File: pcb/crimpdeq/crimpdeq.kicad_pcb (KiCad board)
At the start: 4 copper layers, 30 x 30 mm, 55 parts, among them J10 A-_Cable_Pad, J11 E+_Cable_Pad, J12 E-_Cable_Pad, J2 USB4105-GF-A, J5 B-_Cable_Pad, J6 SW+_Cable_Pad, J7 B+_Cable_Pad, J8 SW-_Cable_Pad, J9 A+_Cable_Pad, Q2 DMG3415U, U1 ESP32-C3-MINI-1, U2 MCP73831T-2ACI/OT, U3 ADS1220, U5 MAX17048G+T10, U6 SY8088

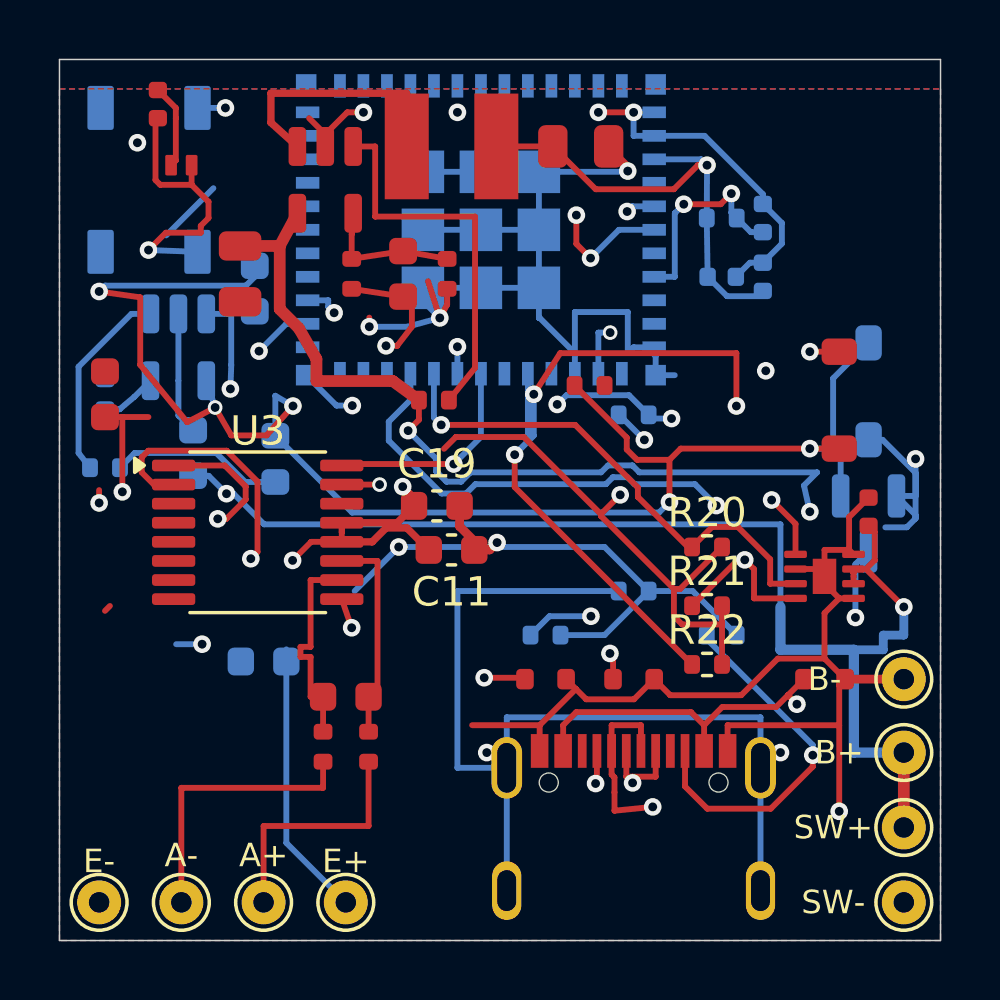
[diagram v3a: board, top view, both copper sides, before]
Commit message: fix: align prototype metadata and clean board annotations
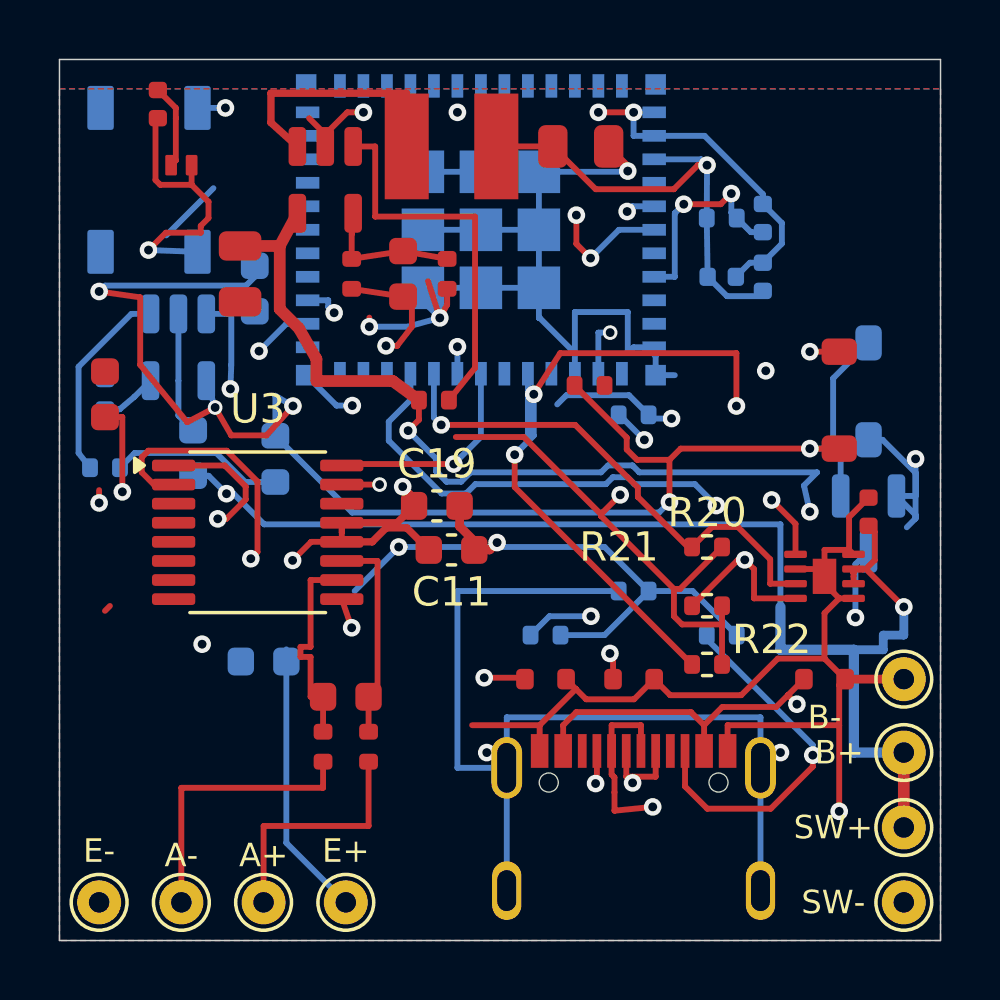
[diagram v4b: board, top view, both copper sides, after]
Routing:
- net +3V3: track 124.8 -> 122.5 mm
- net VSYS: track 41.1 -> 40.3 mm
- net Net-(D4-DIN): vias 4 -> 2
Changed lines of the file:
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@@
 		(sheetname "/")
 		(sheetfile "crimpdeq.kicad_sch")
+		(attr dnp)
 		(duplicate_pad_numbers_are_jumpers no)
 		(fp_circle
@@
 					(thickness 0.08)
 				)
-				(justify mirror)
 			)
 		)
@@
 					(thickness 0.06)
 				)
-				(justify mirror)
 			)
 		)
@@
 					(thickness 0.06)
 				)
-				(justify mirror)
 			)
 		)
@@
 		(tags "TSSOP SO JEDEC-MO-153-AB Texas_PW0016A Microchip-ST Toshiba-TSSOP16-P-0044-0.65A NXP-SOT403-1 Infineon-P-TSSOP-16-800")
 		(property "Reference" "U3"
-			(at 0 -3.45 0)
+			(at 0 -4.2 0)
 			(layer "F.SilkS")
 			(effects
@@
 		(tags "resistor")
 		(property "Reference" "R21"
-			(at 0 -1.17 0)
+			(at -3.0 -2.0 0)
 			(layer "F.SilkS")
 			(effects
@@
 					(thickness 0.04)
 				)
-				(justify mirror)
 			)
 		)
@@
 		(sheetname "/")
 		(sheetfile "crimpdeq.kicad_sch")
+		(attr dnp)
 		(duplicate_pad_numbers_are_jumpers no)
 		(fp_circle
@@
 					(thickness 0.04)
 				)
-				(justify mirror)
 			)
 		)
@@
 		(sheetname "/")
 		(sheetfile "crimpdeq.kicad_sch")
+		(attr dnp)
 		(duplicate_pad_numbers_are_jumpers no)
 		(fp_circle
@@
 					(thickness 0.15)
 				)
-				(justify mirror)
 			)
 		)
@@
 					(thickness 0.04)
 				)
-				(justify mirror)
 			)
 		)
@@
 			)
 		)
+		(attr dnp)
 		(duplicate_pad_numbers_are_jumpers no)
 		(fp_circle
@@
 		(sheetname "/")
 		(sheetfile "crimpdeq.kicad_sch")
+		(attr dnp)
 		(duplicate_pad_numbers_are_jumpers no)
 		(fp_circle
@@
 					(thickness 0.04)
 				)
-				(justify mirror)
 			)
 		)
@@
 					(thickness 0.04)
 				)
-				(justify mirror)
 			)
 		)
@@
 					(thickness 0.04)
 				)
-				(justify mirror)
 			)
 		)
@@
 					(thickness 0.06)
 				)
-				(justify mirror)
 			)
 		)
@@
 			)
 		)
+		(attr dnp)
 		(duplicate_pad_numbers_are_jumpers no)
 		(fp_circle
@@
 					(thickness 0.08)
 				)
-				(justify mirror)
 			)
 		)
@@
 		(tags "resistor")
 		(property "Reference" "R22"
-			(at 0 -1.17 0)
+			(at 2.2 -0.85 0)
 			(layer "F.SilkS")
 			(effects
@@
 		(sheetname "/")
 		(sheetfile "crimpdeq.kicad_sch")
+		(attr dnp)
 		(duplicate_pad_numbers_are_jumpers no)
 		(fp_circle
@@
 		(sheetname "/")
 		(sheetfile "crimpdeq.kicad_sch")
+		(attr dnp)
 		(duplicate_pad_numbers_are_jumpers no)
 		(fp_circle
@@
 					(thickness 0.06)
 				)
+				(justify mirror)
 			)
 		)
@@
 					(thickness 0.04)
 				)
+				(justify mirror)
 			)
 		)
@@
 					(thickness 0.06)
 				)
+				(justify mirror)
 			)
 		)
@@
 					(thickness 0.04)
 				)
+				(justify mirror)
 			)
 		)
@@
 					(thickness 0.04)
 				)
+				(justify mirror)
 			)
 		)
@@
 					(thickness 0.04)
 				)
+				(justify mirror)
 			)
 		)
@@
 					(thickness 0.04)
 				)
+				(justify mirror)
 			)
 		)
@@
 					(thickness 0.04)
 				)
+				(justify mirror)
 			)
 		)
@@
 					(thickness 0.04)
 				)
+				(justify mirror)
 			)
 		)
@@
 					(thickness 0.06)
 				)
+				(justify mirror)
 			)
 		)
@@
 					(thickness 0.06)
 				)
+				(justify mirror)
 			)
 		)
@@
 					(thickness 0.04)
 				)
+				(justify mirror)
 			)
 		)
@@
 	)
 	(gr_text "B-"
-		(at 153.5 73.5 0)
+		(at 153.5 74.8 0)
 		(layer "F.SilkS")
 		(effects
@@
 	)
 	(gr_text "E-"
-		(at 128.8 79.7 0)
+		(at 128.8 79.35 0)
 		(layer "F.SilkS")
 		(effects
@@
 	)
 	(gr_text "E+"
-		(at 137.2 79.7 0)
+		(at 137.2 79.35 0)
 		(layer "F.SilkS")
 		(effects
@@
 	)
 	(segment
-		(start 140.946 65.2556)
-		(end 140.544 65.6573)
-		(width 0.2)
-		(layer "F.Cu")
-		(net "+3V3")
-	)
-	(segment
 		(start 132.525 57.2436)
 		(end 131.95 56.6686)
@@
 	)
 	(segment
-		(start 129.591 64.575)
-		(end 130.48 64.575)
-		(width 0.2)
-		(layer "F.Cu")
-		(net "+3V3")
-	)
-	(segment
 		(start 131.073 58.2984)
 		(end 132.26 58.2984)
@@
 	)
 	(segment
-		(start 131.422 72.31)
-		(end 132.307 72.31)
-		(width 0.2)
-		(layer "B.Cu")
-		(net "+3V3")
-	)
-	(segment
 		(start 149.3 55.8)
 		(end 149.5 56)
@@
 	)
 	(segment
-		(start 156.302 68.3298)
-		(end 155.57 68.3298)
-		(width 0.2)
-		(layer "B.Cu")
-		(net "VSYS")
-	)
-	(segment
 		(start 153.247 66.4591)
 		(end 152.8 66.906099)
@@
 		(size 0.6)
 		(drill 0.3)
-		(layers "F.Cu" "B.Cu")
-		(net "Net-(D4-DIN)")
-	)
-	(via
-		(at 144.398 64.1454)
-		(size 0.6)
-		(drill 0.3)
-		(layers "F.Cu" "B.Cu")
-		(net "Net-(D4-DIN)")
-	)
-	(via
-		(at 130.103 55.2355)
-		(size 0.6)
-		(drill 0.3)

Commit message: fix: remove queued dangling PCB objects
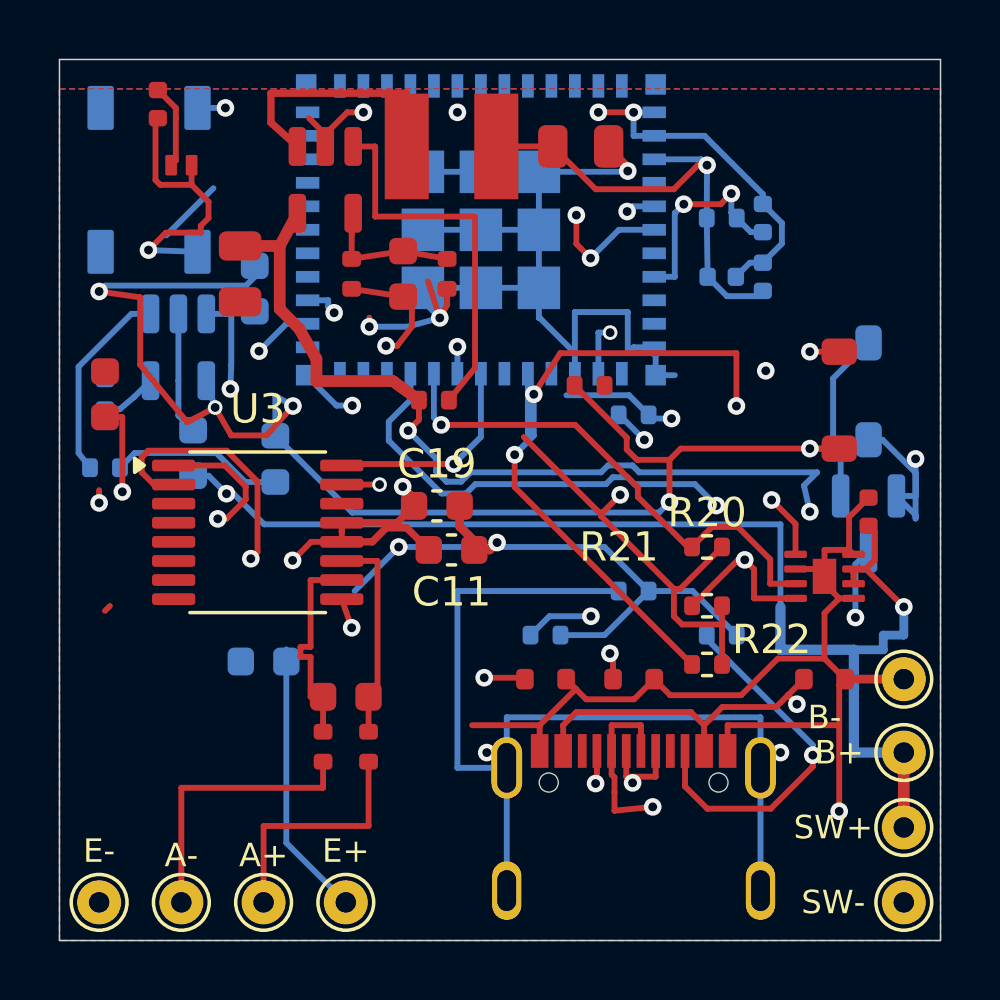
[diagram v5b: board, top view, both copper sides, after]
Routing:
- net +3V3: track 122.5 -> 120.2 mm, vias 9 -> 8
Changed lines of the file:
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@@
-	)
-	(segment
-		(start 143.26 65.2556)
-		(end 140.946 65.2556)
-		(width 0.2)
-		(layer "F.Cu")
-		(net "+3V3")
 	)
 	(segment
@@
 		(net "+3V3")
 	)
-	(via
-		(at 132.307 72.31)
-		(size 0.6)
-		(drill 0.3)
-		(layers "F.Cu" "B.Cu")
-		(net "+3V3")
-	)
 	(segment
 		(start 132.15 58.95)
@@
 	)
 	(segment
-		(start 156.6 68.031)
-		(end 156.302 68.3298)
-		(width 0.2)
-		(layer "B.Cu")
-		(net "VSYS")
-	)
-	(segment
 		(start 140.628 66.7771)
 		(end 140.275 66.4245)
@@
 		(width 0.2)
 		(layer "B.Cu")
-		(net "Net-(D4-DIN)")
-	)
-	(segment
-		(start 144.398 64.1454)
-		(end 144.711 63.8327)
-		(width 0.2)
-		(layer "B.Cu")

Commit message: feat: Prepare missing items
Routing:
- net +3V3: track 120.2 -> 116.5 mm
- net Net-(D4-DIN): track 34.2 -> 32.0 mm
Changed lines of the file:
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@@
 		(sheetname "/")
 		(sheetfile "crimpdeq.kicad_sch")
-		(attr dnp)
+		(attr exclude_from_pos_files dnp)
 		(duplicate_pad_numbers_are_jumpers no)
 		(fp_circle
@@
 		(sheetname "/")
 		(sheetfile "crimpdeq.kicad_sch")
-		(attr dnp)
+		(attr exclude_from_pos_files dnp)
 		(duplicate_pad_numbers_are_jumpers no)
 		(fp_circle
@@
 		(sheetname "/")
 		(sheetfile "crimpdeq.kicad_sch")
-		(attr dnp)
+		(attr exclude_from_pos_files dnp)
 		(duplicate_pad_numbers_are_jumpers no)
 		(fp_circle
@@
 			)
 		)
-		(attr dnp)
+		(attr exclude_from_pos_files dnp)
 		(duplicate_pad_numbers_are_jumpers no)
 		(fp_circle
@@
 		(sheetname "/")
 		(sheetfile "crimpdeq.kicad_sch")
-		(attr dnp)
+		(attr exclude_from_pos_files dnp)
 		(duplicate_pad_numbers_are_jumpers no)
 		(fp_circle
@@
 			)
 		)
-		(attr dnp)
+		(attr exclude_from_pos_files dnp)
 		(duplicate_pad_numbers_are_jumpers no)
 		(fp_circle
@@
 		(sheetname "/")
 		(sheetfile "crimpdeq.kicad_sch")
-		(attr dnp)
+		(attr exclude_from_pos_files dnp)
 		(duplicate_pad_numbers_are_jumpers no)
 		(fp_circle
@@
 		(sheetname "/")
 		(sheetfile "crimpdeq.kicad_sch")
-		(attr dnp)
+		(attr exclude_from_pos_files dnp)
 		(duplicate_pad_numbers_are_jumpers no)
 		(fp_circle
@@
 	)
 	(segment
-		(start 145.886 67.8825)
-		(end 143.26 65.2556)
-		(width 0.2)
-		(layer "F.Cu")
-		(net "+3V3")
-	)
-	(segment
 		(start 135.388 69.4566)
 		(end 136.02 68.825)
@@
 		(width 0.2)
 		(layer "B.Cu")
-		(net "Net-(D4-DIN)")
-	)
-	(segment
-		(start 144.711 63.8327)
-		(end 146.843 63.8327)
-		(width 0.2)
-		(layer "B.Cu")
